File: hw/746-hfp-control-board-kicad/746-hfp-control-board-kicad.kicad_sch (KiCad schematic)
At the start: 11 parts, among them J16 Control_board_Connector, SW1 SW_Push, SW4 SW_SPST

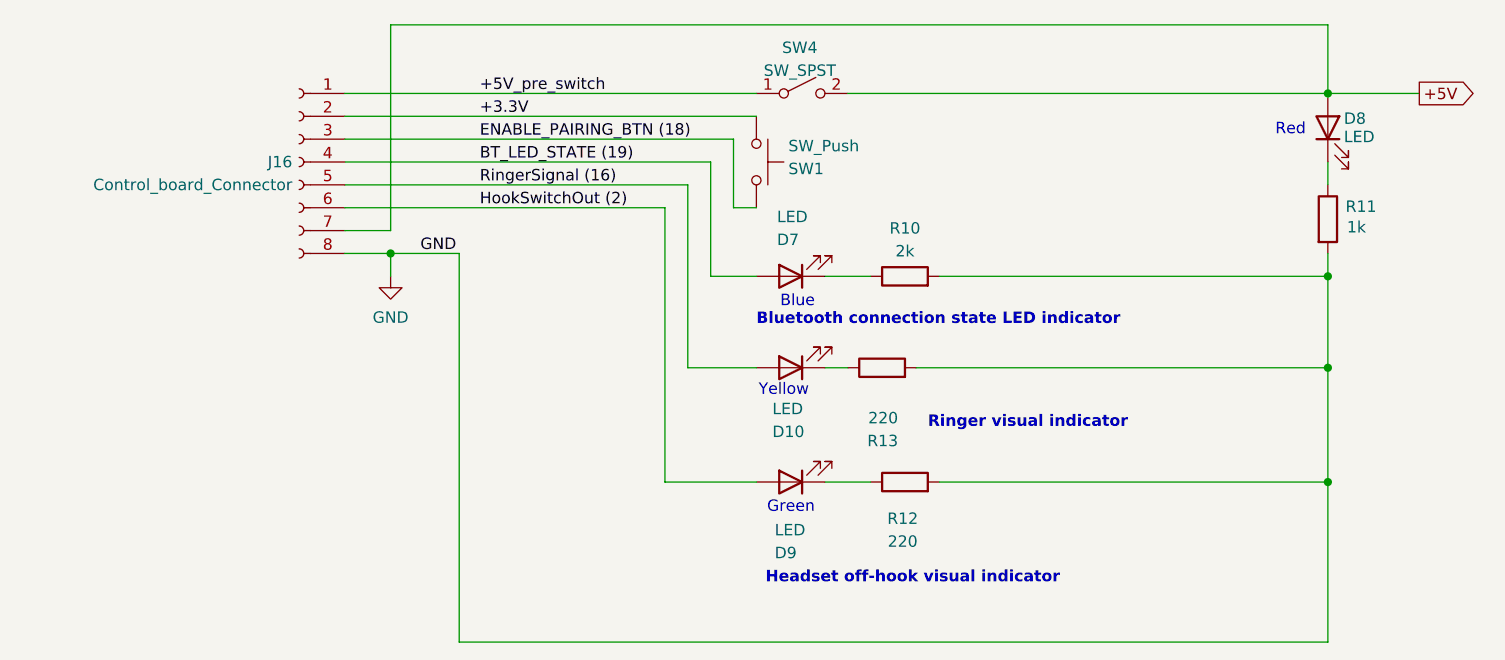
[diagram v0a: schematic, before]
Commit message: Add schematic & pcb for control board
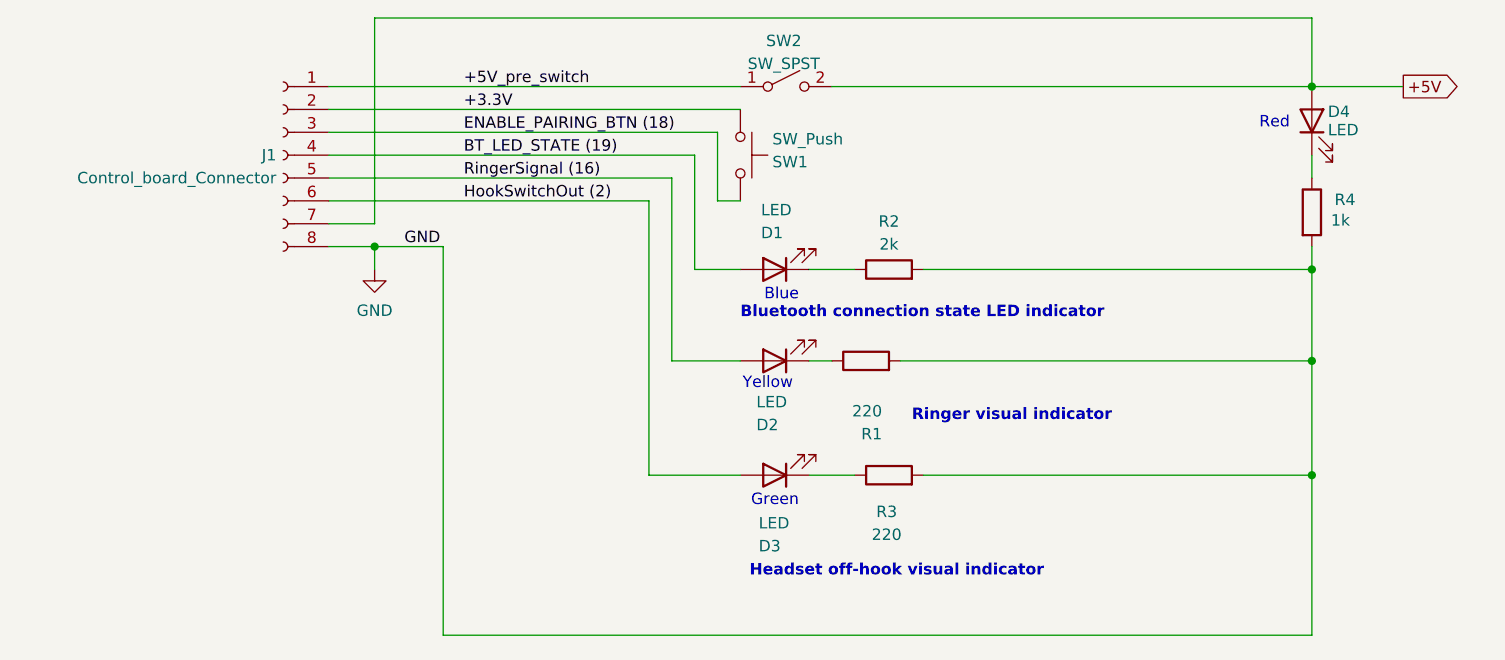
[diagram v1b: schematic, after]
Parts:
- removed D10, D7, D8, D9: LED, LED_THT:LED_D5.0mm, symbol Device:LED
- removed J16: Control_board_Connector, Connector_PinSocket_2.54mm:PinSocket_1x15_P2.54mm_Vertical, symbol Connector:Conn_01x08_Socket
- removed R10: 2k, Resistor_THT:R_Axial_DIN0207_L6.3mm_D2.5mm_P10.16mm_Horizontal, symbol Device:R
- removed R11: 1k, Resistor_THT:R_Axial_DIN0207_L6.3mm_D2.5mm_P10.16mm_Horizontal, symbol Device:R
- removed R12, R13: 220, Resistor_THT:R_Axial_DIN0207_L6.3mm_D2.5mm_P10.16mm_Horizontal, symbol Device:R
- removed SW4: SW_SPST, Connector_PinHeader_2.54mm:PinHeader_1x02_P2.54mm_Vertical, symbol Switch:SW_SPST
- added D1, D2, D3, D4: LED, LED_THT:LED_D5.0mm, symbol Device:LED
- added J1: Control_board_Connector, Connector_PinSocket_2.54mm:PinSocket_1x08_P2.54mm_Vertical, symbol Connector:Conn_01x08_Socket
- added R1, R3: 220, Resistor_THT:R_Axial_DIN0207_L6.3mm_D2.5mm_P10.16mm_Horizontal, symbol Device:R
- added R2: 2k, Resistor_THT:R_Axial_DIN0207_L6.3mm_D2.5mm_P10.16mm_Horizontal, symbol Device:R
- added R4: 1k, Resistor_THT:R_Axial_DIN0207_L6.3mm_D2.5mm_P10.16mm_Horizontal, symbol Device:R
- added SW2: SW_SPST, Connector_PinHeader_2.54mm:PinHeader_1x02_P2.54mm_Vertical, symbol Switch:SW_SPST
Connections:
- net +3.3V: now also J1.2 (Pin_2)
- net +5V: now also D4.2 (A), J1.7 (Pin_7), SW2.2 (B)
- net +5V_pre_switch: now also J1.1 (Pin_1), SW2.1 (A)
- net BT_LED_STATE (19): now also D1.2 (A), J1.4 (Pin_4)
- net ENABLE_PAIRING_BTN (18): now also J1.3 (Pin_3)
- net GND: now also J1.8 (Pin_8), R1.2, R2.2, R3.2, R4.2
- net HookSwitchOut (2): now also D3.2 (A), J1.6 (Pin_6)
- net RingerSignal (16): now also D2.2 (A), J1.5 (Pin_5)
- new net: D1.1 (K), R2.1
- new net: D4.1 (K), R4.1
- new net: D2.1 (K), R1.1
- new net: D3.1 (K), R3.1
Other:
- company: (none) -> Vlad Balmos
- title: (none) -> GPO-746-Bluetooth-conversion Control board
